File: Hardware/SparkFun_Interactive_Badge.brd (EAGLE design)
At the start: 17.8 x 63.5 mm, 36 parts, among them Q1 DMG2307L, U1 MIC5205-3.3V, U2 ATMEGA328P, U3 CY7C65213, Y1 4MHz

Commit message: More re-routing for v11 of the BadgerStick.
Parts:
- removed JP4: M15LOCK_NO_SILK, SparkFun-Connectors:1X15_LOCK_NO_SILK
- added J1: (no value), SparkFun-Connectors:JST-2-SMD
- added JP2: (no value), SparkFun-Connectors:1X15_LOCK_NO_SILK
- added R5, R6: 1K, SparkFun-Resistors:0603-RES
- JP3: value M15LOCK_NO_SILK -> (none); device SparkFun-Connectors:1X15_LOCK_NO_SILK -> SparkFun-Connectors:1X12_LOCK_NO_SILK
- U2: value ATMEGA328P -> ATMEGA328P_TQFP
- moved JP3 31.8 mm to (16.5, 34.3), turned to 270 degrees
- moved LOGO2 14.8 mm to (-7.34, 59.6)
- moved LOGO1 13.0 mm to (24.5, 53.0)
- moved C4 8.28 mm to (4.45, 42.5)
- moved U3 5.59 mm to (8.89, 50.0)
- moved C7 5.08 mm to (2.54, 51.4)
- moved R2 4.45 mm to (6.35, 42.5), turned to 270 degrees
- moved FID2 4.02 mm to (16.5, 53.3)
- moved D2 2.54 mm to (6.35, 38.1)
- moved JP1 2.54 mm to (8.89, 61.0)
- moved C8 1.27 mm to (15.2, 47.6), turned to 270 degrees
- turned C2 to 90 degrees
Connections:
- new net N$3: R5.1, U3.1
- new net N$7: R6.1, U3.5
- net 3.3V: now also JP2.14; no longer JP4.2
- net 5V: now also JP2.15; no longer JP4.1
- net A0: now also JP3.8; no longer JP4.11
- net A1: now also JP3.7; no longer JP4.10
- net A2: now also JP3.6; no longer JP4.9
- net A3: now also JP3.5; no longer JP4.8
- net A4: now also JP3.4; no longer JP4.7
- net A5: now also JP3.3; no longer JP4.6
- net D10: now also JP3.12; no longer JP4.15, JP6.1
- net D2: now also JP2.8; no longer JP3.8
- net D3: now also JP2.7; no longer JP3.7
- net D4: now also JP2.6; no longer JP3.6
- net D5: now also JP2.5; no longer JP3.5
- net D6: now also JP2.4; no longer JP3.4
- net D7: now also JP2.3; no longer JP3.3
- net D8: now also JP2.2; no longer JP3.2
- net D9: now also JP2.1; no longer JP3.1
- net DTR: now also JP2.13; no longer JP3.13
- net GND: now also J1.1, JP2.9, JP3.2; no longer JP3.14, JP3.9, JP4.3
- net MISO: now also JP3.10; no longer JP4.13
- net MOSI: now also JP3.11; no longer JP4.14, JP6.3
- net RESET: now also JP2.10; no longer JP3.10, JP4.4
- net RXI: now also JP2.11, JP6.1, R5.2; no longer JP3.11, U3.1
- net SCK: now also JP3.9; no longer JP4.12
- net TXO: now also JP2.12, JP6.3, R6.2; no longer JP3.12, U3.5
- net VBAT: now also J1.2; no longer JP3.15
- net VCC: now also JP3.1; no longer JP4.5
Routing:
- net RXI: track 38.7 -> 89.8 mm, vias 1 -> 3
- net 5V: track 47.4 -> 65.5 mm, vias 0 -> 1
- net DTR: track 26.5 -> 13.1 mm
- net RESET: track 82.1 -> 69.7 mm, vias 3 -> 2
- net MOSI: track 32.8 -> 23.5 mm
- net N$7: track 0.00 -> 9.20 mm
- net GND: track 17.3 -> 8.22 mm, vias 26 -> 14
- net VBAT: track 25.1 -> 17.6 mm, vias 1 -> 2
- net TXO: track 32.7 -> 25.4 mm
- net D10: track 29.2 -> 24.4 mm
- net N$3: track 0.00 -> 4.23 mm
- net MISO: track 21.7 -> 25.6 mm
- net VCC: track 48.6 -> 51.7 mm
- net D+: track 11.6 -> 8.97 mm
- net 3.3V: track 48.3 -> 46.3 mm
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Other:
- board size 17.8 x 63.5 mm -> 17.8 x 66 mm
- board text added: "0"
- board text added: "1"
- board text removed: "RXI"
- board text removed: "TXO"

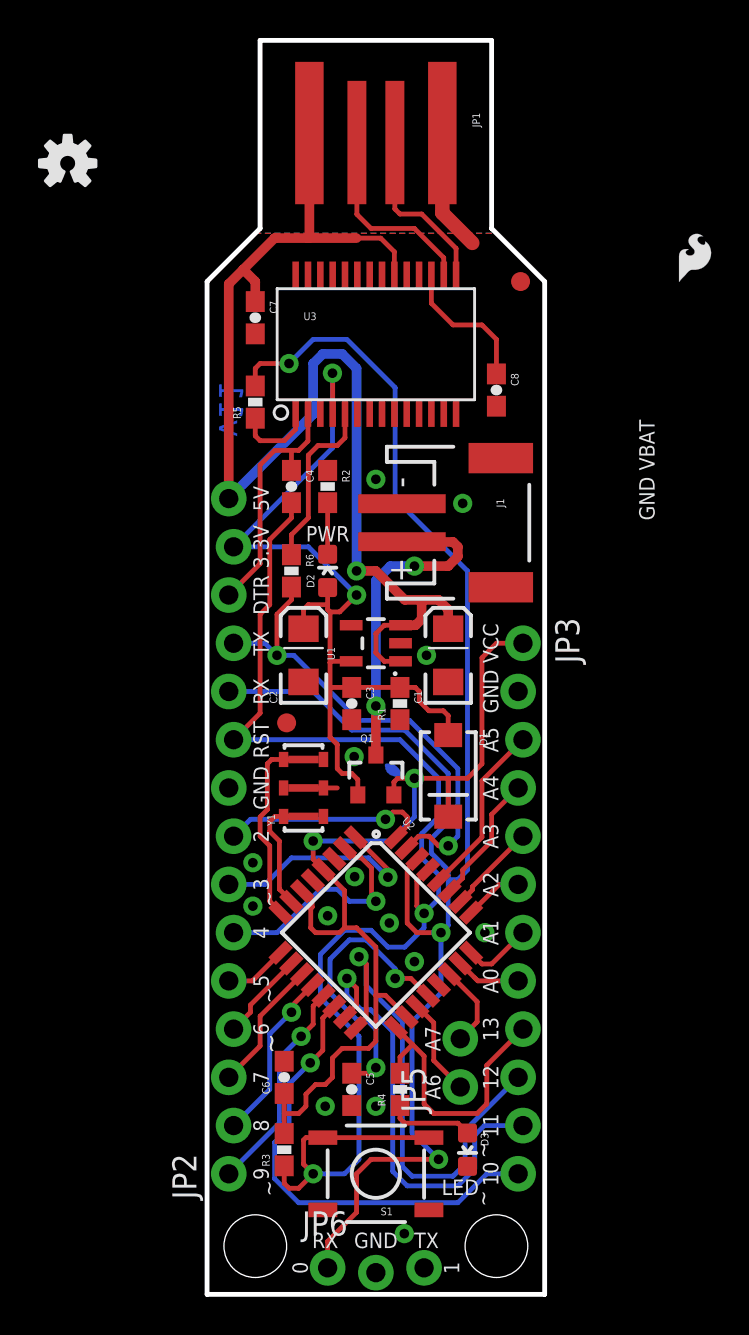
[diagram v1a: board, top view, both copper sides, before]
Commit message: Finished new layout with JST, inline resistors (UART), and 0/1 pin game port.
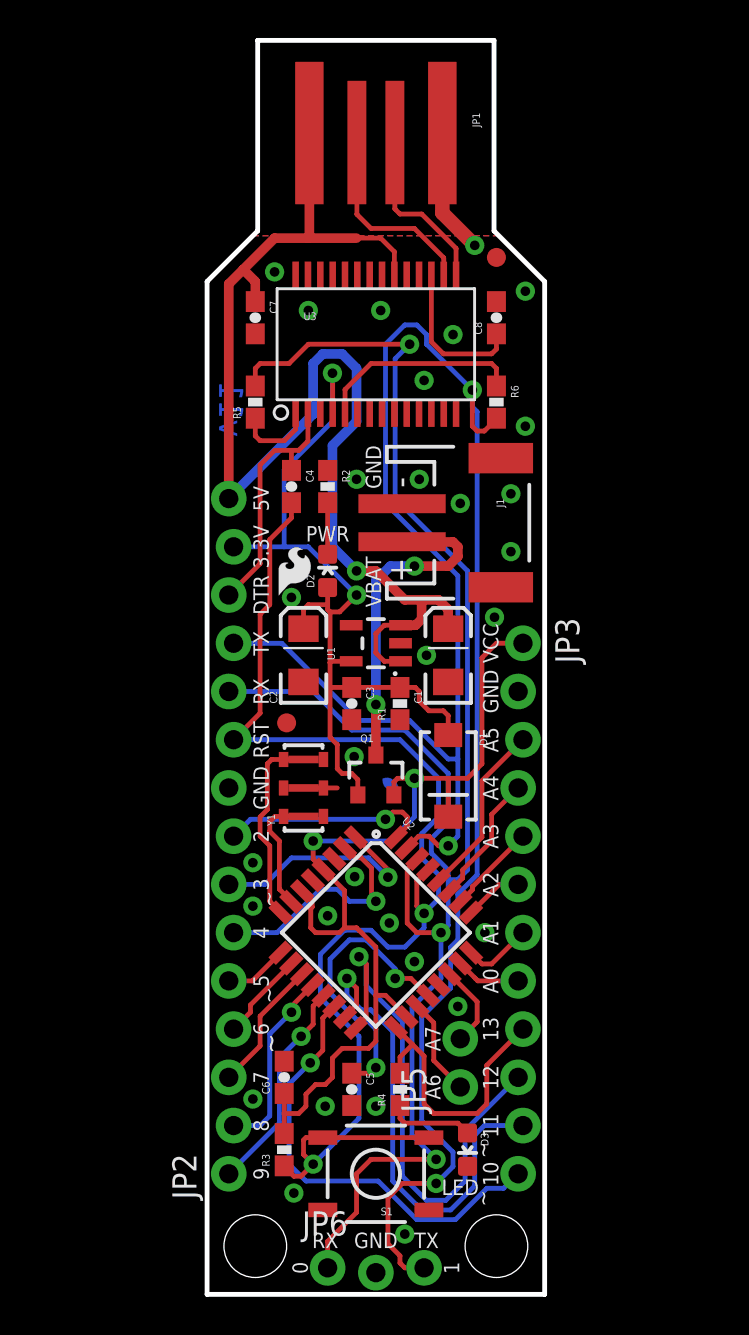
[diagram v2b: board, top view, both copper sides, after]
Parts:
- moved LOGO1 26.8 mm to (3.45, 36.4)
- moved LOGO2 24.9 mm to (8.89, 40.6), flipped to the bottom
- moved R6 14.0 mm to (15.2, 47.0)
- moved C8 3.81 mm to (15.2, 51.4), turned to 90 degrees
- moved FID2 1.80 mm to (15.2, 54.6)
- moved U$3 0.77 mm to (12.6, 19.6)
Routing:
- net TXO: track 25.4 -> 107.6 mm, vias 2 -> 3
- net RESET: track 69.7 -> 66.9 mm
- net RXI: track 89.8 -> 91.8 mm
- net MOSI: track 23.5 -> 25.4 mm
- net MISO: track 25.6 -> 27.5 mm
- net N$7: track 9.20 -> 10.8 mm
- net 3.3V: track 46.3 -> 45.2 mm
- net 5V: track 65.5 -> 66.5 mm
- net D8: track 9.14 -> 9.96 mm
- net D10: track 24.4 -> 23.6 mm
- net N$2: track 7.53 -> 8.13 mm
- net GND: vias 14 -> 30
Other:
- outline, holes or cut-outs redrawn
- board text added: "Serial Port"
- board text removed: "Battery"
- board text removed: "Game Port"

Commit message: Adjusted vias to allow for 2 connections to GND from 328p. Moved silk slightly to avoid vias (as possible).
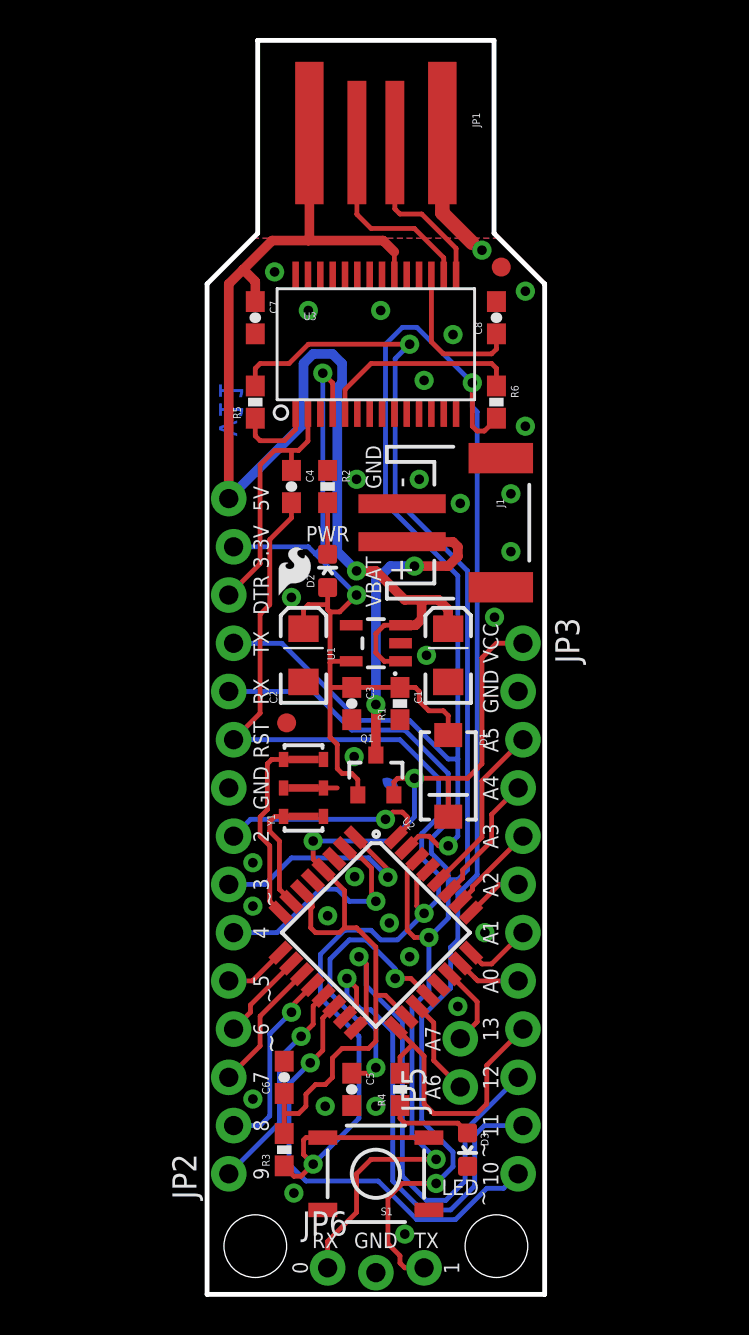
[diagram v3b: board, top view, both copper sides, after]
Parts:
- moved LOGO2 0.76 mm to (8.89, 39.9)
- moved FID2 0.57 mm to (15.5, 54.1)
- moved U$1 0.51 mm to (14.9, 45.2)
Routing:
- net 5V: track 66.5 -> 65.7 mm
- net RESET: track 66.9 -> 66.1 mm
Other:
- outline, holes or cut-outs redrawn

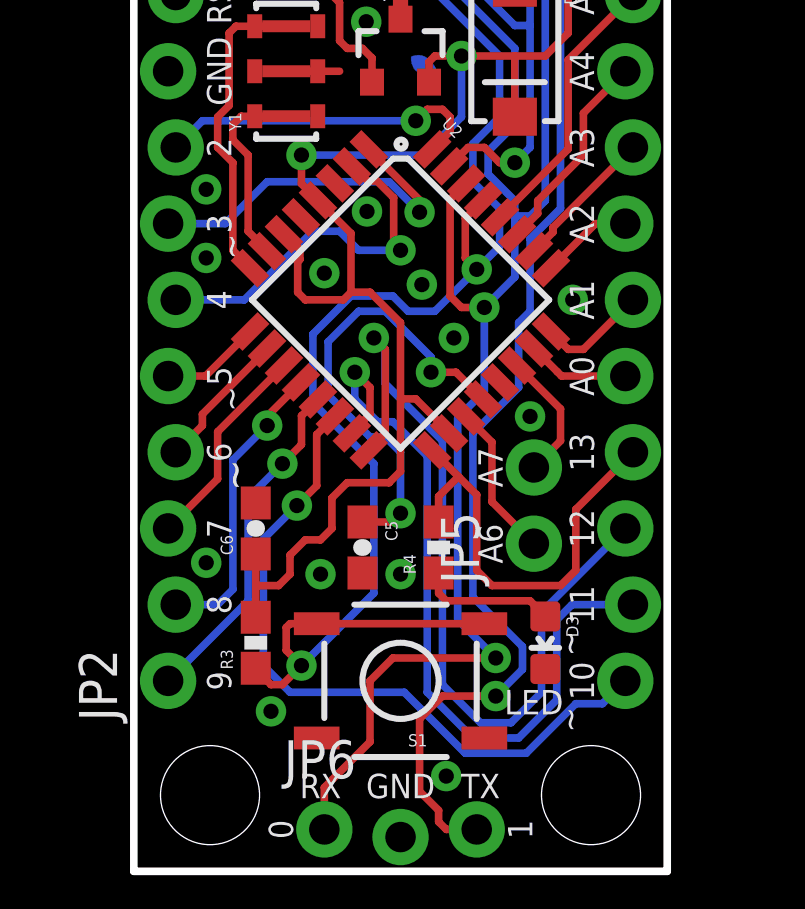
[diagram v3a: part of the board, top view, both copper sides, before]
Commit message: Changed LED silk to '13'. Added notes to sch about voltage range and JST connector. Moved wire in sch for VCC on 328p to avoid confusion with the RESET line.
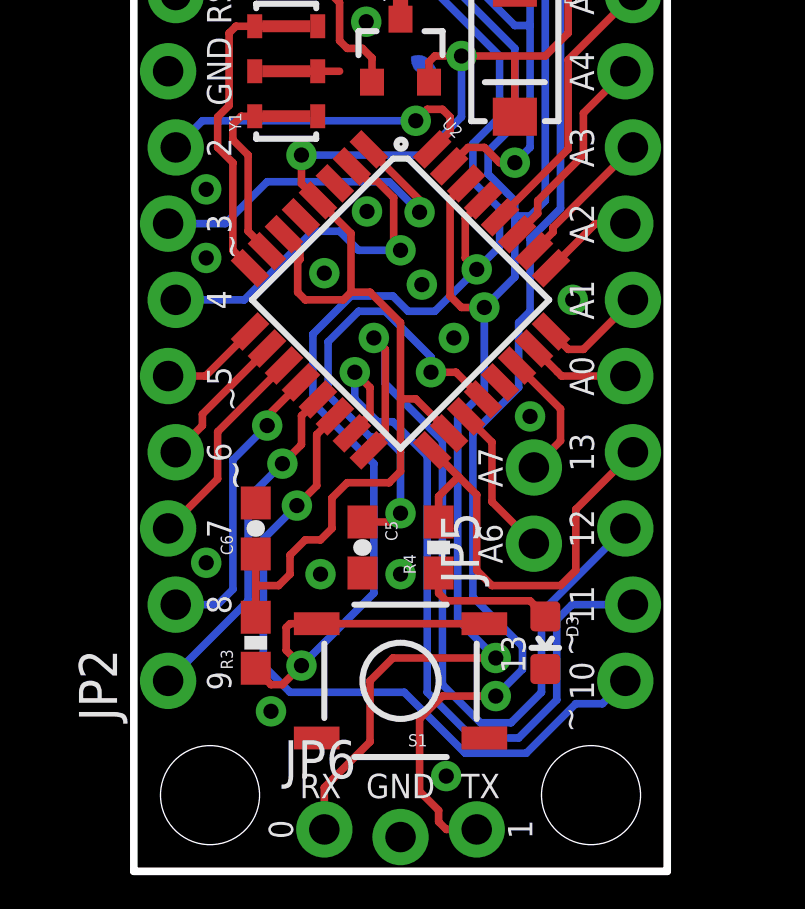
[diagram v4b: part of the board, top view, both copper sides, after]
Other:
- board text added: "All measurements in inches"
- board text removed: "LED"
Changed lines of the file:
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@@
 <setting verticaltext="up"/>
 </settings>
-<grid distance="0.05" unitdist="inch" unit="inch" style="dots" multiple="1" display="yes" altdistance="0.005" altunitdist="inch" altunit="inch"/>
+<grid distance="0.01" unitdist="inch" unit="inch" style="dots" multiple="1" display="yes" altdistance="0.005" altunitdist="inch" altunit="inch"/>
 <layers>
 <layer number="1" name="Top" color="4" fill="1" visible="yes" active="yes"/>
@@
 <dimension x1="16.383" y1="3.683" x2="18.669" y2="5.969" x3="19.05" y3="5.969" textsize="1.778" textratio="15" layer="47" dtype="leader" unit="inch"/>
 <text x="19.304" y="5.969" size="1.778" layer="47" ratio="15" align="center-left">0.13</text>
-<text x="13.335" y="5.2324" size="0.8128" layer="21" font="vector" ratio="15" align="bottom-center">LED</text>
+<text x="13.0556" y="7.239" size="0.8128" layer="21" font="vector" ratio="15" rot="R90" align="bottom-center">13</text>
 <text x="6.35" y="39.6494" size="0.8128" layer="21" font="vector" ratio="15" align="bottom-center">PWR</text>
 <dimension x1="-54.61" y1="1.27" x2="-54.61" y2="29.21" x3="-58.42" y3="15.24" textsize="1.778" textratio="15" layer="47" dtype="vertical" unit="inch"/>
@@
 <dimension x1="2.667" y1="66.04" x2="15.113" y2="66.04" x3="8.89" y3="68.58" textsize="1.778" textratio="15" layer="47" dtype="horizontal" unit="inch"/>
 <dimension x1="15.113" y1="55.88" x2="16.256" y2="0" x3="35.56" y3="27.94" textsize="1.778" textratio="15" layer="47" dtype="vertical" unit="inch"/>
+<text x="-50.8" y="-24.13" size="1.778" layer="47" font="vector" ratio="15">All measurements in inches</text>
 </plain>
 <attributes>
@@
 <wire x1="5.588" y1="22.917684375" x2="5.588" y2="23.876" width="0.254" layer="1"/>
 <wire x1="5.588" y1="23.876" x2="9.652" y2="23.876" width="0.254" layer="16"/>
-<contactref element="U2" pad="6"/>
-<contactref element="U2" pad="4"/>
-<contactref element="U2" pad="18"/>
 <contactref element="JP3" pad="1"/>
 <via x="10.922" y="27.178" extent="1-16" drill="0.508"/>
@@
 <wire x1="14.478" y1="33.528" x2="15.24" y2="34.29" width="0.254" layer="1"/>
 <wire x1="15.24" y1="34.29" x2="16.637" y2="34.29" width="0.254" layer="1"/>
-<wire x1="6.137515625" y1="22.36816875" x2="7.239" y2="21.266684375" width="0.254" layer="1"/>
-<wire x1="5.588" y1="22.917684375" x2="6.137515625" y2="22.36816875" width="0.254" layer="1"/>
 <wire x1="12.7" y1="25.155" x2="12.7" y2="27.178" width="0.254" layer="1"/>
-<wire x1="5.00614375" y1="21.236796875" x2="5.026803125" y2="21.236796875" width="0.254" layer="1"/>
-<wire x1="5.026803125" y1="21.236796875" x2="5.5372" y2="20.7264" width="0.254" layer="1"/>
-<wire x1="10.5111125" y1="14.600459375" x2="10.5111125" y2="14.6348875" width="0.254" layer="1"/>
+<wire x1="5.1308" y1="21.1328" x2="5.5372" y2="20.7264" width="0.254" layer="1"/>
 <wire x1="10.5111125" y1="14.6348875" x2="9.398" y2="15.748" width="0.254" layer="1"/>
 <wire x1="8.89" y1="15.748" x2="8.89" y2="13.335" width="0.254" layer="1"/>
+<contactref element="U2" pad="4"/>
+<contactref element="U2" pad="6"/>
+<contactref element="U2" pad="18"/>
+<wire x1="6.137515625" y1="22.36816875" x2="5.588" y2="22.917684375" width="0.254" layer="1"/>
+<wire x1="6.137515625" y1="22.36816875" x2="7.239" y2="21.266684375" width="0.254" layer="1"/>
+<wire x1="10.5111125" y1="14.600459375" x2="10.5111125" y2="14.6348875" width="0.254" layer="1"/>
+<wire x1="5.00614375" y1="21.236796875" x2="5.026803125" y2="21.236796875" width="0.254" layer="1"/>
+<wire x1="5.026803125" y1="21.236796875" x2="5.1308" y2="21.1328" width="0.254" layer="1"/>
 </signal>
 <signal name="3.3V">
